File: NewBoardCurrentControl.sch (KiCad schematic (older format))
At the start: 21 parts, among them Q401 RSR030N06TL, U401 ADA4528-2ACPZ-RL, U402 782853152_WE-CBA_08

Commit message: revise AtoD
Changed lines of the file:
@@
 Wire Wire Line
 	6750 4450 6750 4850
-Text Label 8550 4850 0    50   ~ 0
-VOLTAGE
 Connection ~ 6750 4850
 $Comp
@@
 Wire Wire Line
 	6750 4850 7100 4850
-Connection ~ 7100 4850
-Wire Wire Line
-	7100 4850 8550 4850
 $Comp
 L power:GND #PWR0402

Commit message: add mod symbol
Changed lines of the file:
@@
 	0    1    1    0
 $EndComp
-Text Label 3600 3850 2    50   ~ 0
-MODULATION_SIGNAL
 Wire Wire Line
 	3600 3650 3600 3850
@@
 Text Label 10500 1900 2    50   ~ 0
 To_Laser
+Text HLabel 3600 3850 0    50   Input ~ 0
+MODULATION_SIGNAL
 $EndSCHEMATC

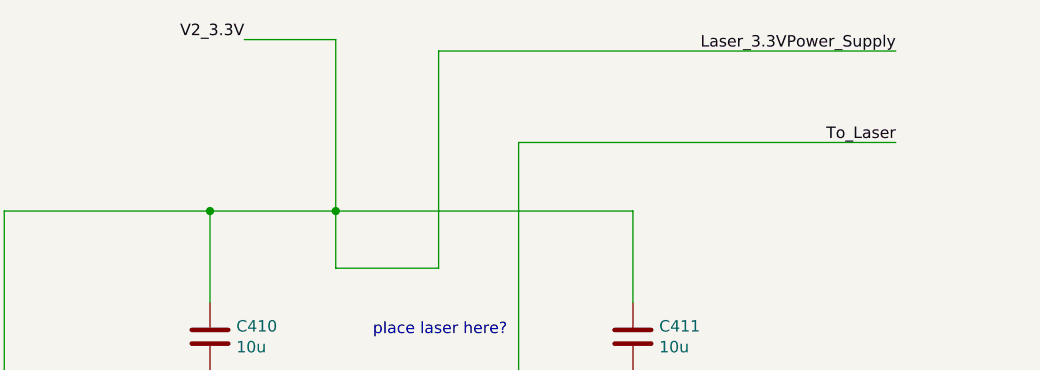
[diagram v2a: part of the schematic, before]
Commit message: added more ports
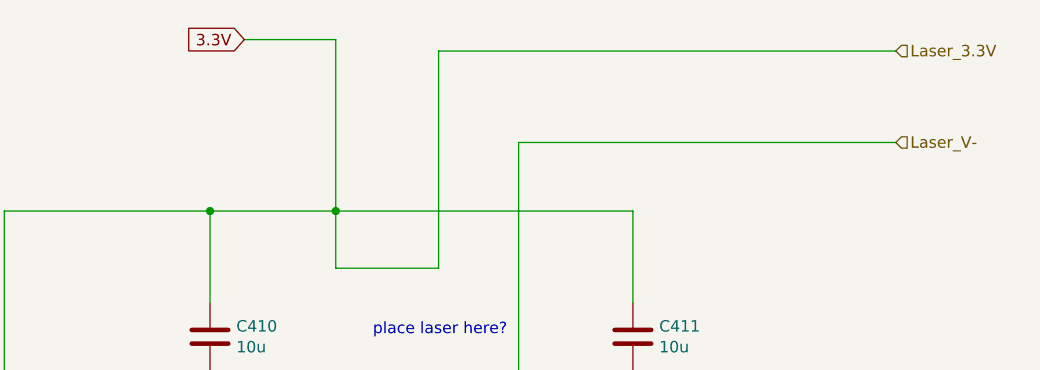
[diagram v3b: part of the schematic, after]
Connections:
- net Laser_3.3VPower_Supply renamed 3.3V
- net To_Laser renamed Laser_V-
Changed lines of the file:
@@
 Text Notes 8800 2750 2    50   ~ 0
 place laser here?\n
-Text Label 7650 1450 2    50   ~ 0
-V2_3.3V
 $Comp
 L Y16070R50000F9W:Y16070R50000F9W R407
@@
 	8850 1900 10500 1900
 Connection ~ 8050 3050
-Text Label 10500 1500 2    50   ~ 0
-Laser_3.3VPower_Supply
-Text Label 10500 1900 2    50   ~ 0
-To_Laser
 Text HLabel 3600 3850 0    50   Input ~ 0
 MODULATION_SIGNAL
+Text HLabel 10500 1500 2    50   Input ~ 0
+Laser_3.3V
+Text HLabel 10500 1900 2    50   Input ~ 0
+Laser_V-
+Text GLabel 7650 1450 0    50   Input ~ 0
+3.3V
 $EndSCHEMATC

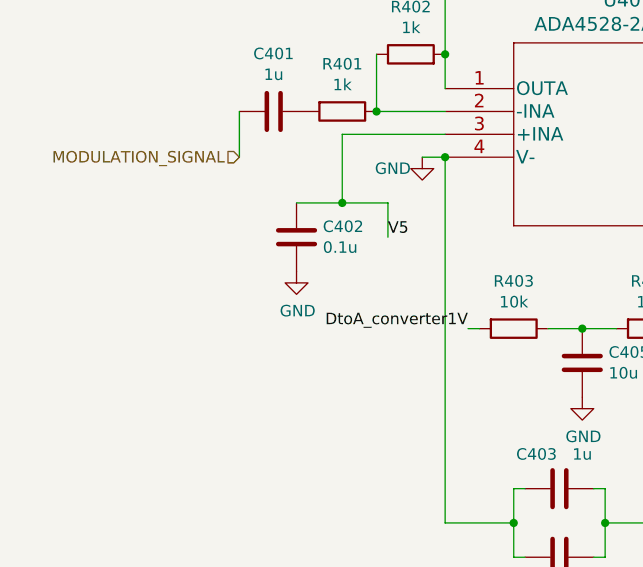
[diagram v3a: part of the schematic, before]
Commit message: adding labels
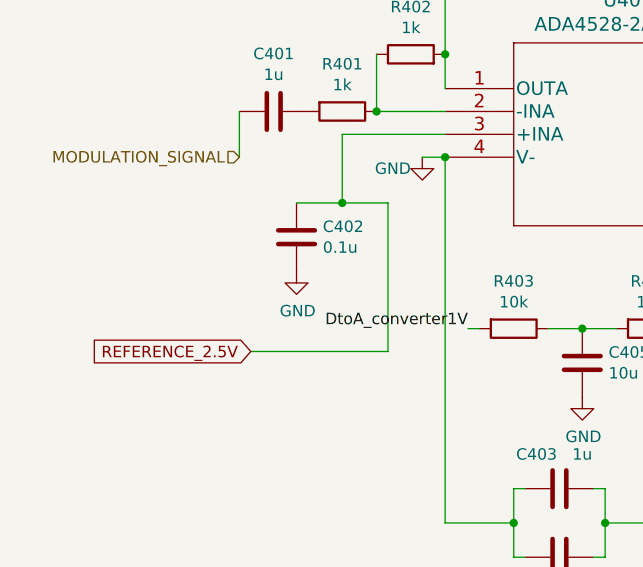
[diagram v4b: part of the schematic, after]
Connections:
- net V5 renamed REFERENCE_2.5V
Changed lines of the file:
@@
 Wire Wire Line
 	4050 4050 4250 4050
-Wire Wire Line
-	4250 4050 4250 4200
 Connection ~ 4050 4050
-Text Label 4250 4200 0    50   ~ 0
-V5
 Connection ~ 8050 3700
 $Comp
@@
 Text GLabel 7650 1450 0    50   Input ~ 0
 3.3V
+Text GLabel 3650 4700 0    50   Input ~ 0
+REFERENCE_2.5V
+Wire Wire Line
+	4250 4700 3650 4700
+Wire Wire Line
+	4250 4050 4250 4700
 $EndSCHEMATC
